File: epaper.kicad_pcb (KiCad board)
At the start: 2 copper layers, 50 x 35 mm, 38 parts, among them Q1 Q_NMOS_GSD, U1 SC18IS602B, U2 e-paper

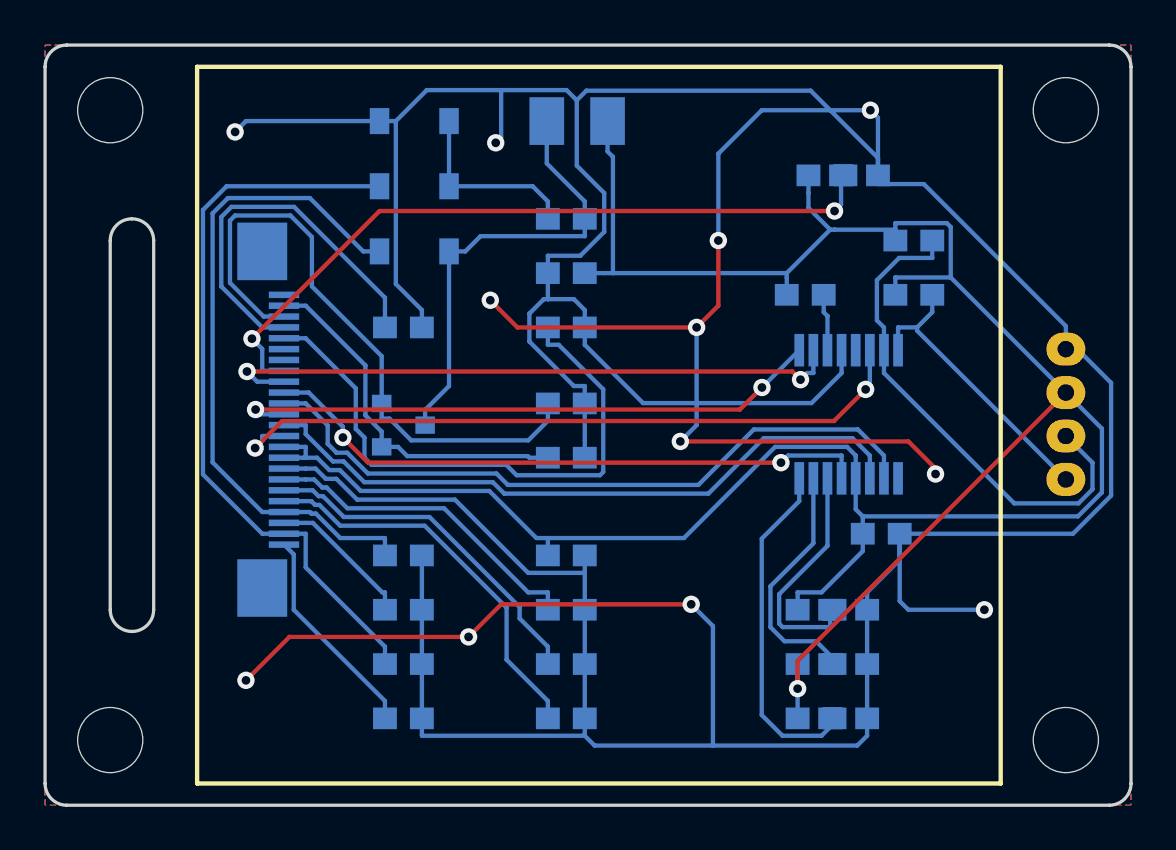
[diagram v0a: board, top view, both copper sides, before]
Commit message: Fix the position of the HFL Connector
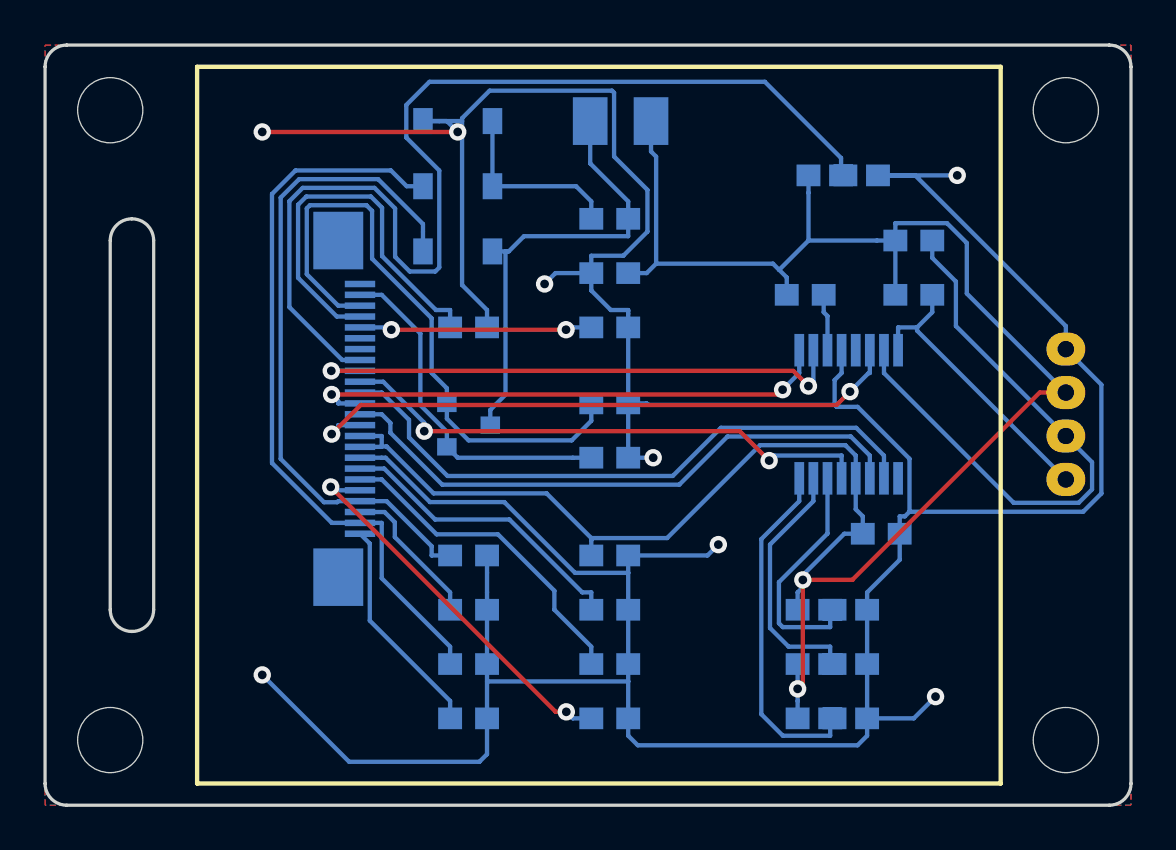
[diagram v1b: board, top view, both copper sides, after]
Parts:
- moved U2 3.54 mm to (157.5, 132.5)
- moved C10 3.00 mm to (162.5, 123.0)
- moved C11 3.00 mm to (162.5, 138.5)
- moved C13 3.00 mm to (162.5, 141.0)
- moved C8 3.00 mm to (162.5, 133.5)
- moved C9 3.00 mm to (162.5, 136.0)
- moved Q1 3.00 mm to (162.5, 127.5)
- moved C12 2.00 mm to (169.0, 123.0)
- moved C2 2.00 mm to (169.0, 120.5)
- moved C3 2.00 mm to (169.0, 118.0)
- moved C4 2.00 mm to (169.0, 133.5)
- moved C5 2.00 mm to (169.0, 136.0)
- moved C6 2.00 mm to (169.0, 138.5)
- moved C7 2.00 mm to (169.0, 141.0)
- moved D1 2.00 mm to (162.0, 113.5)
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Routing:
- net GND: track 262.4 -> 187.4 mm, vias 12 -> 8
- net /3.3V: track 121.9 -> 101.0 mm, vias 1 -> 2
- net /eBS: track 33.9 -> 50.3 mm, vias 2 -> 0
- net Net-(C12-Pad1): track 27.0 -> 10.7 mm, vias 0 -> 2
- net /SDA: track 23.5 -> 27.9 mm
- net /eMOSI: track 32.8 -> 28.5 mm
- net /eBUSY: track 29.3 -> 25.3 mm
- net /eDC: track 32.3 -> 28.7 mm
- net /eCLK: track 31.0 -> 27.4 mm
- net /eRST: track 28.5 -> 25.1 mm
- net /eCS: track 27.6 -> 24.5 mm
- net Net-(C5-Pad1): track 15.1 -> 13.8 mm
- net Net-(C6-Pad1): track 16.2 -> 15.2 mm
- net /RESE: track 29.2 -> 28.5 mm
- net /GDR: track 16.8 -> 16.1 mm
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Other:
- board text added: "e-Paper I2C Module v1.1 1804 Crescent"
- board text removed: "e-Paper I2C Module v1.0 1803 Crescent"
